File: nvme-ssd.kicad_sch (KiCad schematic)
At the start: 20 parts

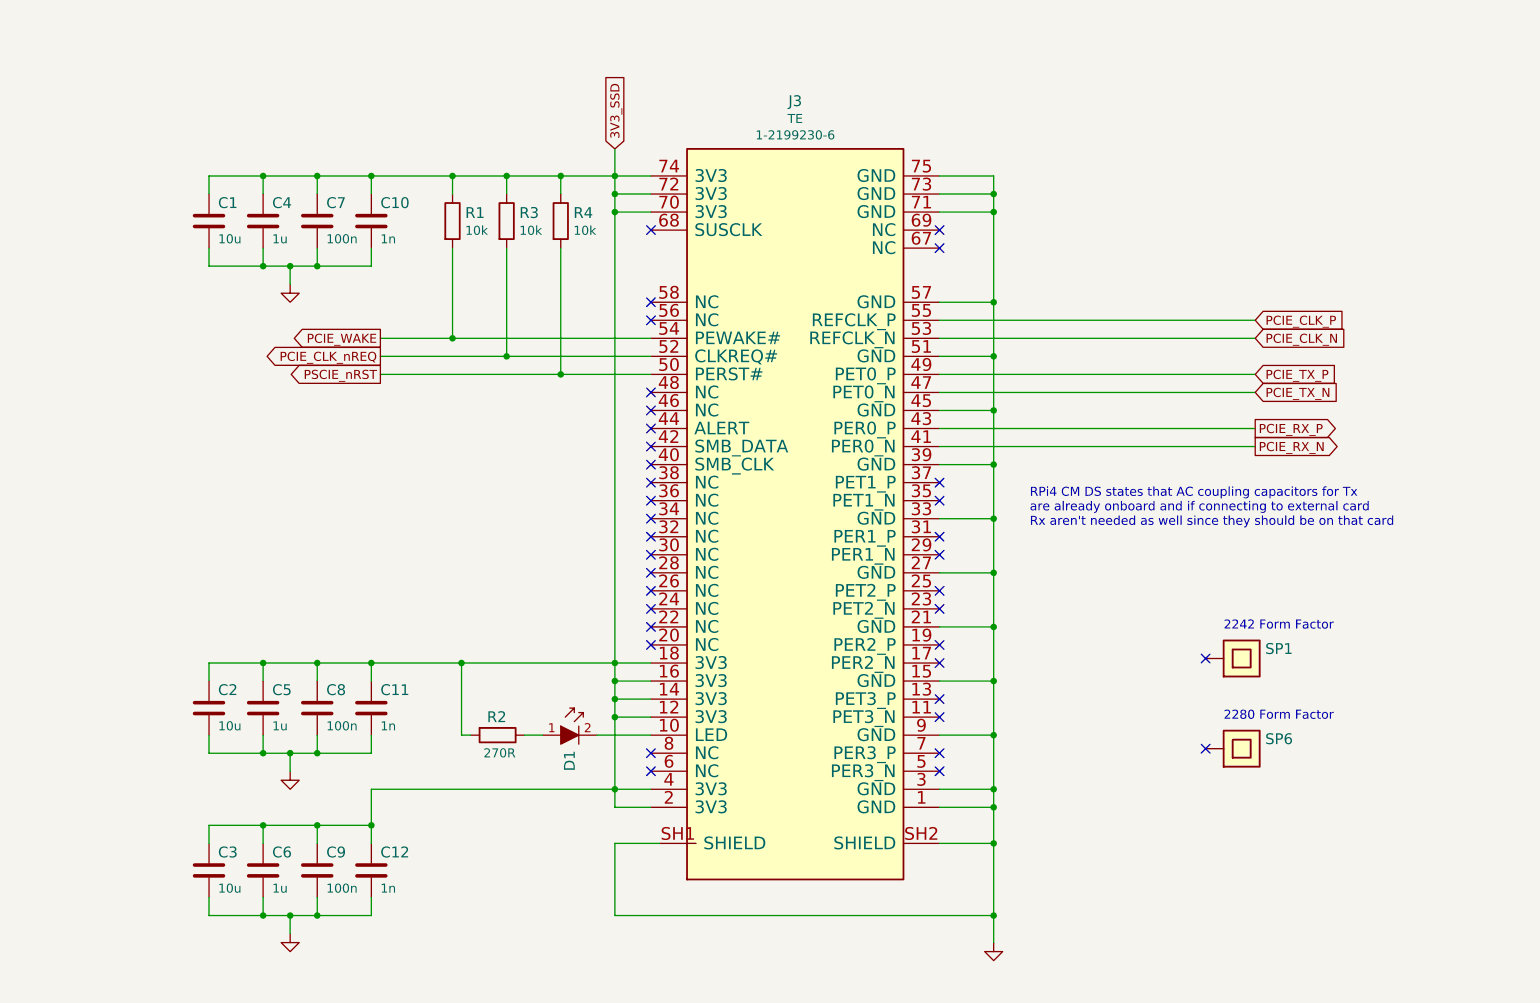
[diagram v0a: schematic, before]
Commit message: Exchanged flyback to CUI DCDC converter on schematics. Added logos.
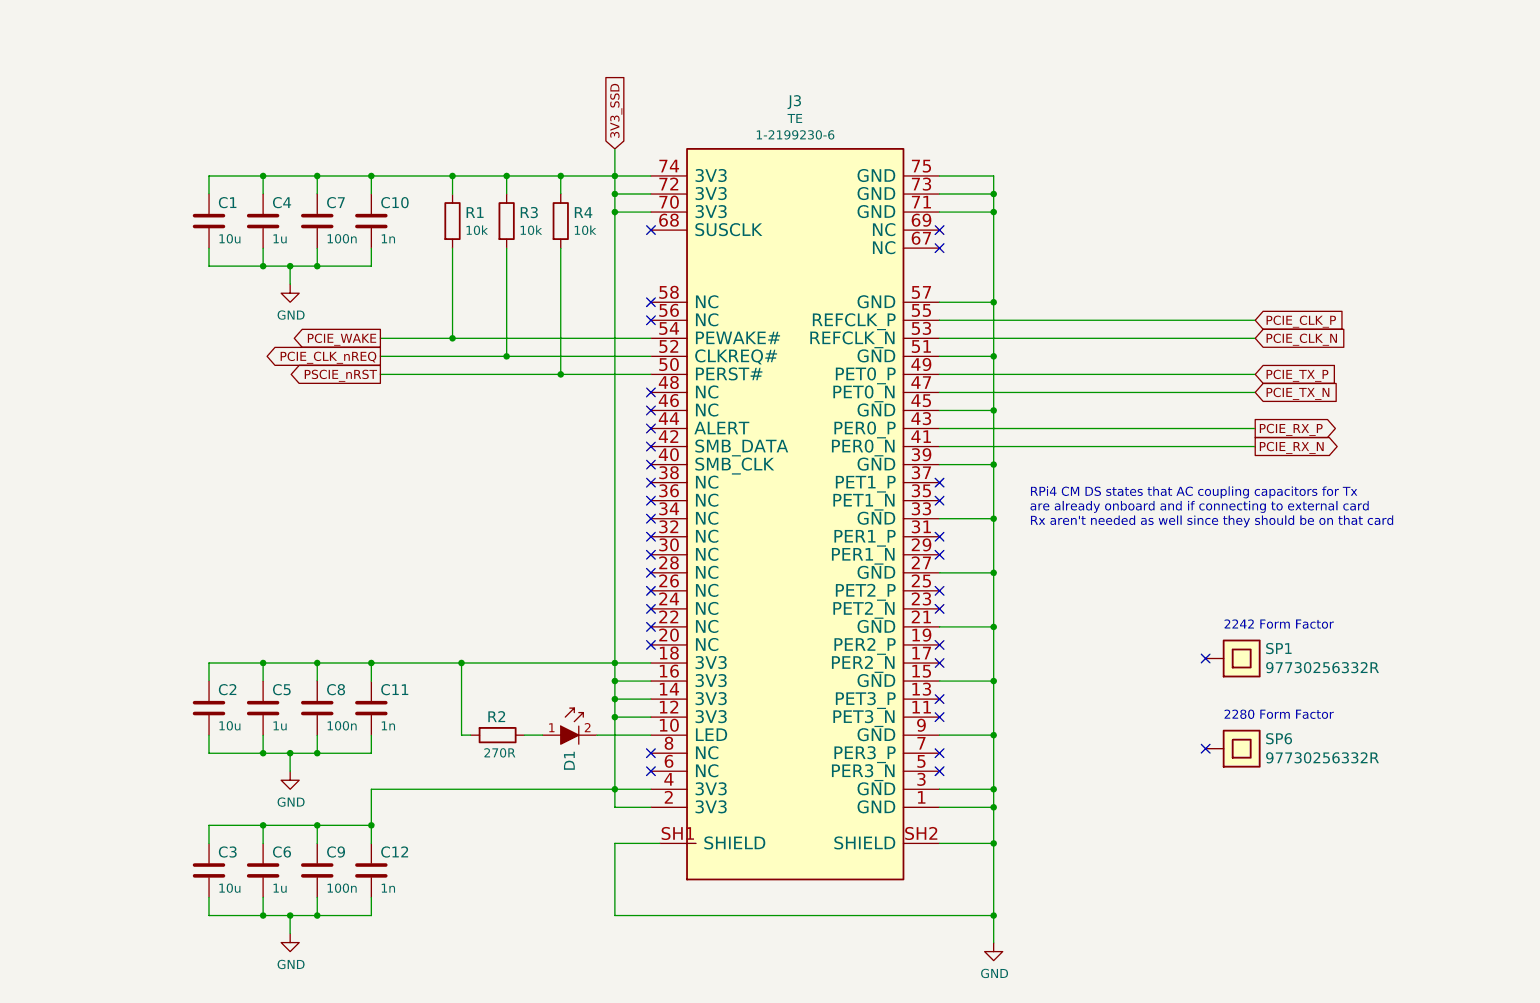
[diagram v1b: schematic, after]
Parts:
- C1, C2, C3: value (none) -> C_10u_0603; footprint scalenode-footprints: -> scalenode-footprints:0603-cap
- C10, C11, C12: value (none) -> C_1n_0603; footprint scalenode-footprints: -> scalenode-footprints:0603-cap
- C4, C5, C6: value (none) -> C_1u_0603; footprint scalenode-footprints: -> scalenode-footprints:0603-cap
- C7, C8, C9: value (none) -> C_100n_0603; footprint scalenode-footprints: -> scalenode-footprints:0603-cap
- D1: value (none) -> KP-1608CGCK; footprint scalenode-footprints: -> scalenode-footprints:LED_0603
- J3: value (none) -> 1-2199230-6; footprint scalenode-footprints: -> scalenode-footprints:1-2199230-6
- R1, R3, R4: value (none) -> R_10k_0603; footprint scalenode-footprints: -> scalenode-footprints:0603-res
- R2: value (none) -> R_270R_0603; footprint scalenode-footprints: -> scalenode-footprints:0603-res
- SP1, SP6: value (none) -> 97730256332R; footprint scalenode-footprints: -> scalenode-footprints:97730256332R

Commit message: Added text fields with schematic descriptions
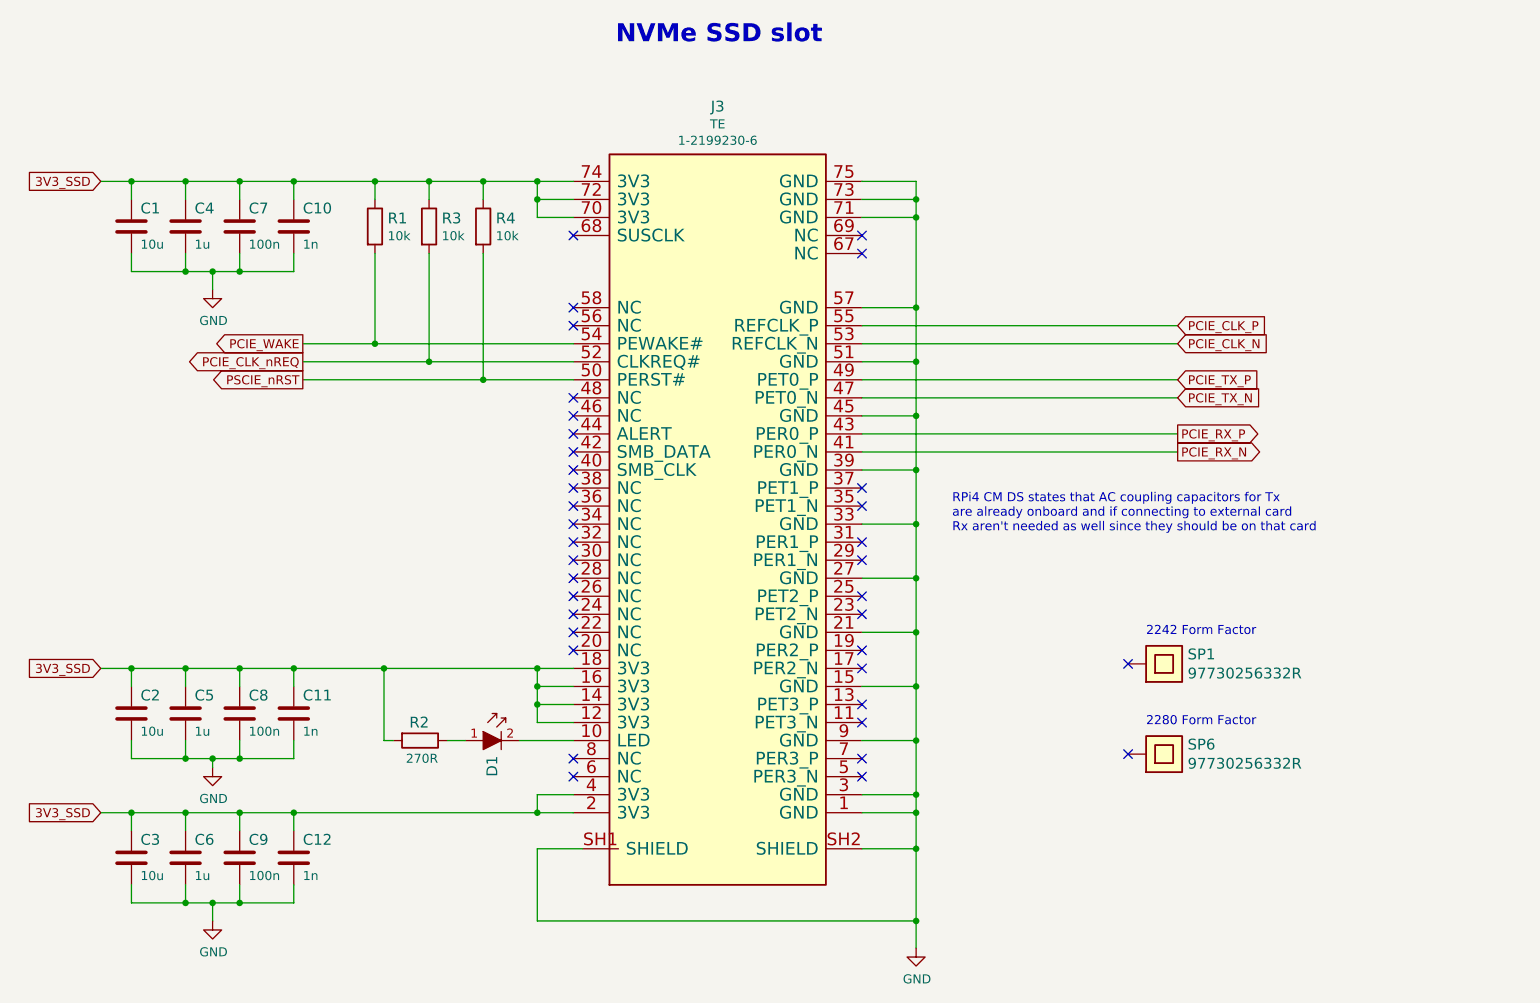
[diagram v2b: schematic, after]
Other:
- note added: "NVMe SSD slot"
- moved on the sheet: C1, C10, C11, C12, C2, C3, C4, C5, C6, C7, C8, C9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

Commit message: Implemented changes from rev 1.0.4. New components initial placement
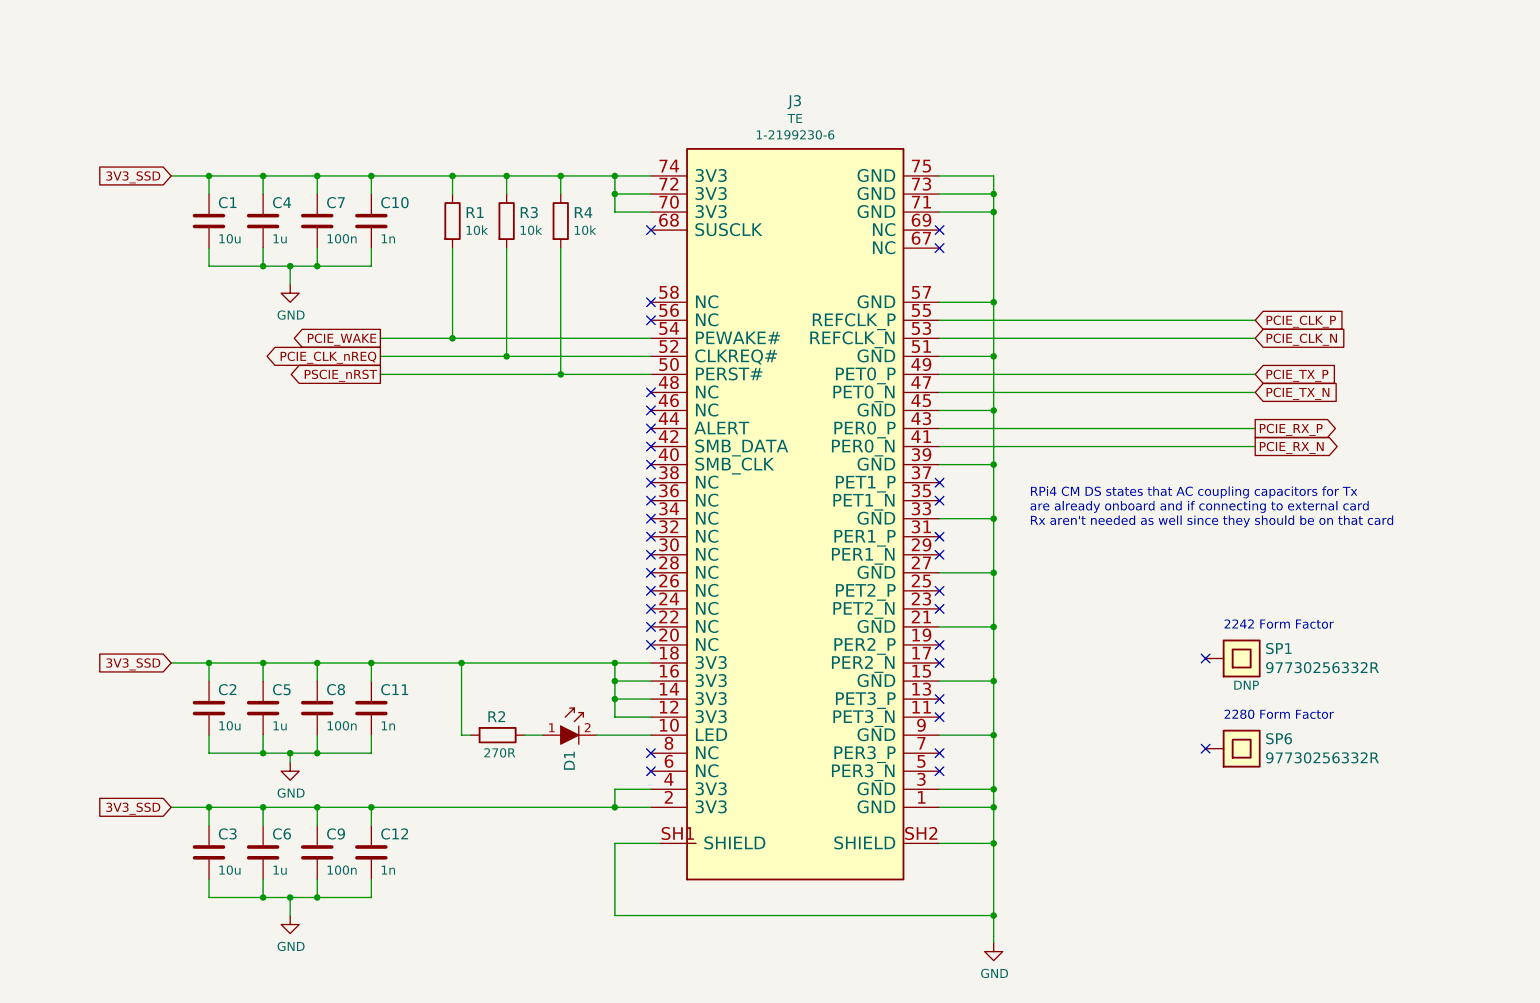
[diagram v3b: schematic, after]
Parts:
- removed D1: KP-1608CGCK, scalenode-footprints:LED_0603, symbol scalenode:KP-1608CGCK
- added D1: 598-8D80-107F, scalenode-footprints:LED_0603_R, symbol scalenode:598-8D80-107F
- SP1: DNP (none) -> DNP
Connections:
- net at J3.10 (LED): now also D1.2
- net at R2.1: now also D1.1
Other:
- note removed: "NVMe SSD slot"
- moved on the sheet: C1, C10, C11, C12, C2, C3, C4, C5, C6, C7, C8, C9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

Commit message: Rename project files
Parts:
- C1, C2, C3: footprint scalenode-footprints:0603-cap -> scalenode-cm4-baseboard-footprints:0603-cap; symbol scalenode:C_10u_0603 -> scalenode-cm4-baseboard:C_10u_0603
- C10, C11, C12: footprint scalenode-footprints:0603-cap -> scalenode-cm4-baseboard-footprints:0603-cap; symbol scalenode:C_1n_0603 -> scalenode-cm4-baseboard:C_1n_0603
- C4, C5, C6: footprint scalenode-footprints:0603-cap -> scalenode-cm4-baseboard-footprints:0603-cap; symbol scalenode:C_1u_0603 -> scalenode-cm4-baseboard:C_1u_0603
- C7, C8, C9: footprint scalenode-footprints:0603-cap -> scalenode-cm4-baseboard-footprints:0603-cap; symbol scalenode:C_100n_0603 -> scalenode-cm4-baseboard:C_100n_0603
- D1: footprint scalenode-footprints:LED_0603_R -> scalenode-cm4-baseboard-footprints:LED_0603_R; symbol scalenode:598-8D80-107F -> scalenode-cm4-baseboard:598-8D80-107F
- J3: footprint scalenode-footprints:1-2199230-6 -> scalenode-cm4-baseboard-footprints:1-2199230-6; symbol scalenode:1-2199230-6 -> scalenode-cm4-baseboard:1-2199230-6
- R1, R3, R4: footprint scalenode-footprints:0603-res -> scalenode-cm4-baseboard-footprints:0603-res; symbol scalenode:R_10k_0603 -> scalenode-cm4-baseboard:R_10k_0603
- R2: footprint scalenode-footprints:0603-res -> scalenode-cm4-baseboard-footprints:0603-res; symbol scalenode:R_270R_0603 -> scalenode-cm4-baseboard:R_270R_0603
- SP1, SP6: footprint scalenode-footprints:97730256332R -> scalenode-cm4-baseboard-footprints:97730256332R; symbol scalenode:97730256332R -> scalenode-cm4-baseboard:97730256332R
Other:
- title: Scalenode -> Scalenode CM4 Baseboard
